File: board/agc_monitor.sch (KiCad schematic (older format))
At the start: 0 parts

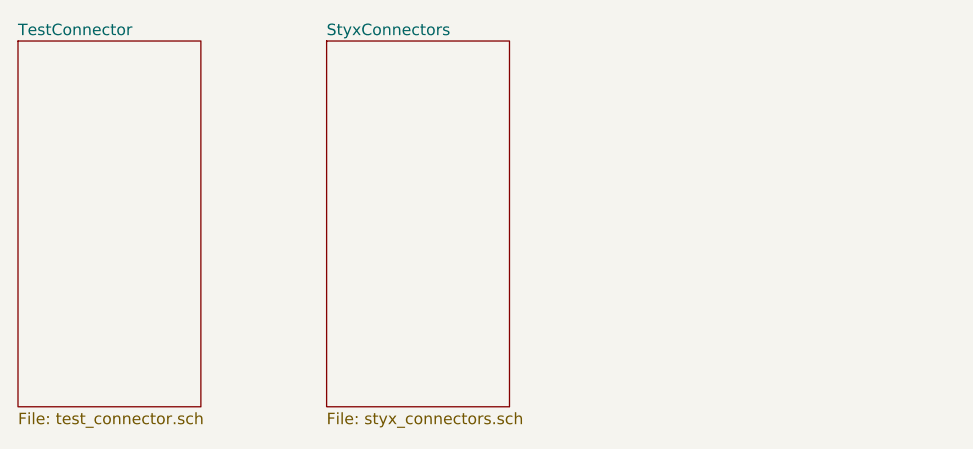
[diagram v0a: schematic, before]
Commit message: Board: initial schematic for the monitor interface board
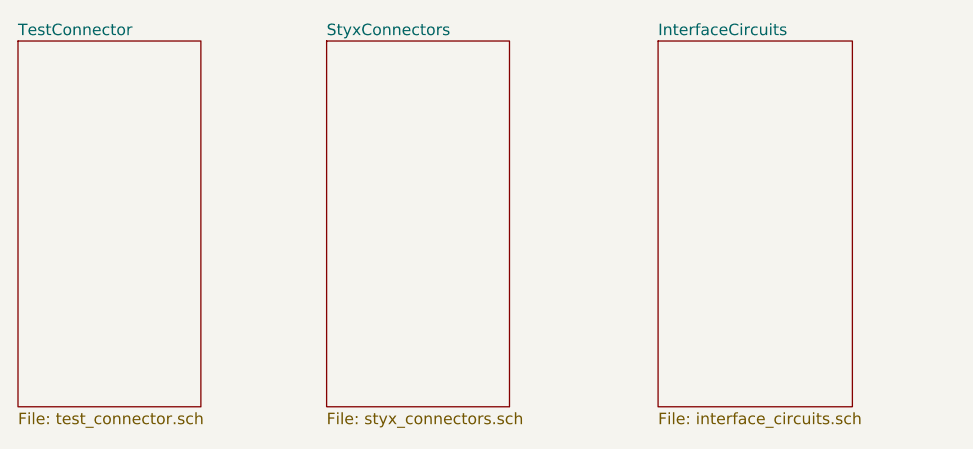
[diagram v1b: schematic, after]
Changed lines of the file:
@@
 $Descr A4 11693 8268
 encoding utf-8
-Sheet 1 3
+Sheet 1 4
 Title ""
 Date ""
@@
 F1 "styx_connectors.sch" 50
 $EndSheet
+$Sheet
+S 4900 1500 850  1600
+U 5C6AE91D
+F0 "InterfaceCircuits" 50
+F1 "interface_circuits.sch" 50
+$EndSheet
 $EndSCHEMATC
